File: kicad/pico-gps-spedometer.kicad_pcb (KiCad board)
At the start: 2 copper layers, 19 parts, among them J1 Akkumulátor be, J2 TP4056-18650-Charger, J3 uBlox NEO GPS (6M/8M), Q1 PN2222A, U1 RP2040-ZERO, U2 DS18B20, U3 LM7805_TO220, U4 TFT_320x240

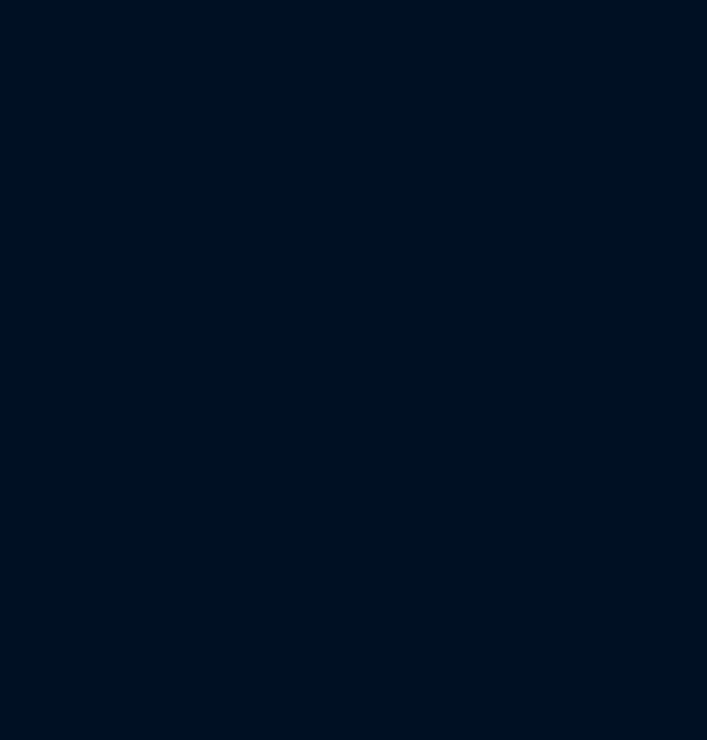
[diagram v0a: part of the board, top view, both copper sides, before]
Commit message: Add TFT backlight adjustment and utility functions
- Implemented TftBackLightAdjuster for dynamic LED backlight control based on ambient light sensor readings.
- Added utility functions for TFT touch calibration and sound feedback (beepTick and beepError) in Utils.cpp.
- Included necessary headers and defined constants for sensor thresholds and brightness levels.
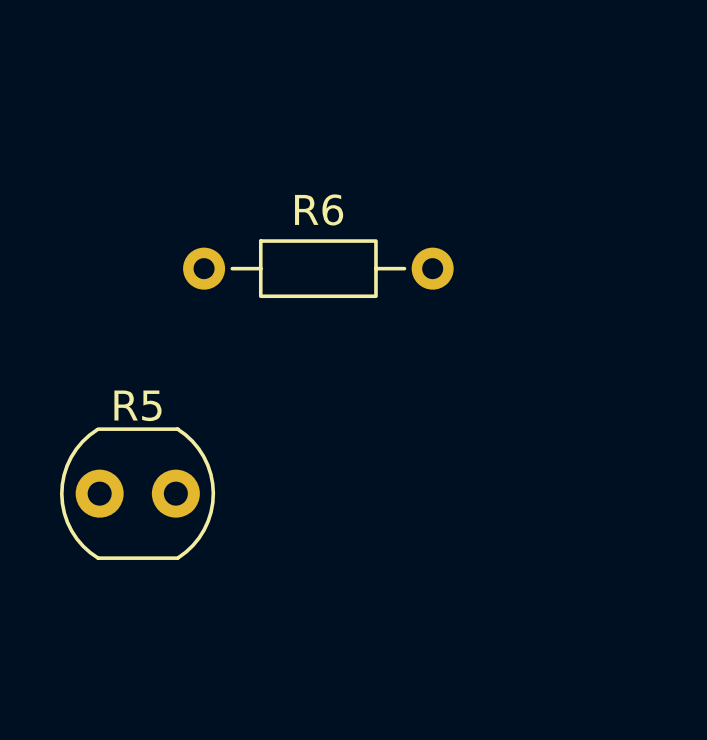
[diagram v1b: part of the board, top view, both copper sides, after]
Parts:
- added R5: GL5516, OptoDevice:R_LDR_4.9x4.2mm_P2.54mm_Vertical, F.Cu at (91.5, 110.0)
- added R6: 10k, Resistor_THT:R_Axial_DIN0204_L3.6mm_D1.6mm_P7.62mm_Horizontal, F.Cu at (94.9, 102.5)
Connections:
- U1 pad 18: unconnected-(U1-GP27-Pad18) -> Net-(U1-GP27)

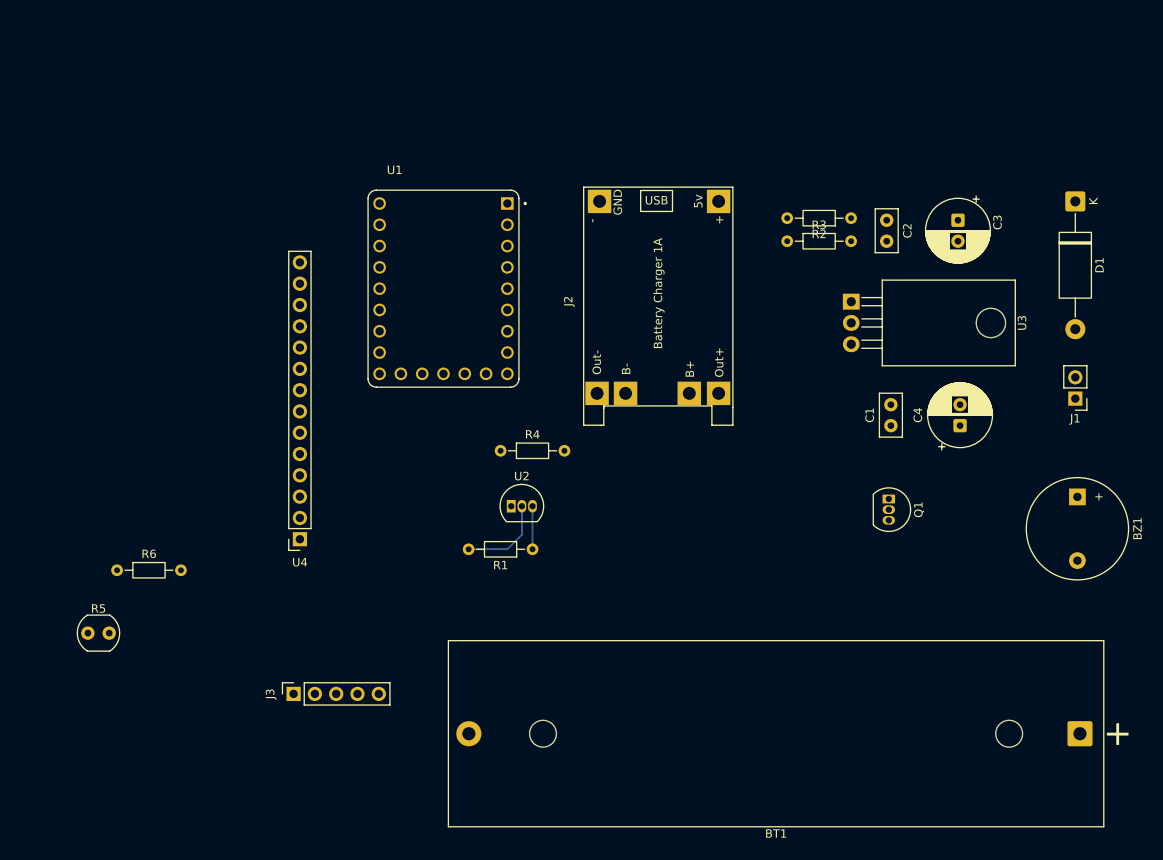
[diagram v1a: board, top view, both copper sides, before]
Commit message: egyoldalas nyák
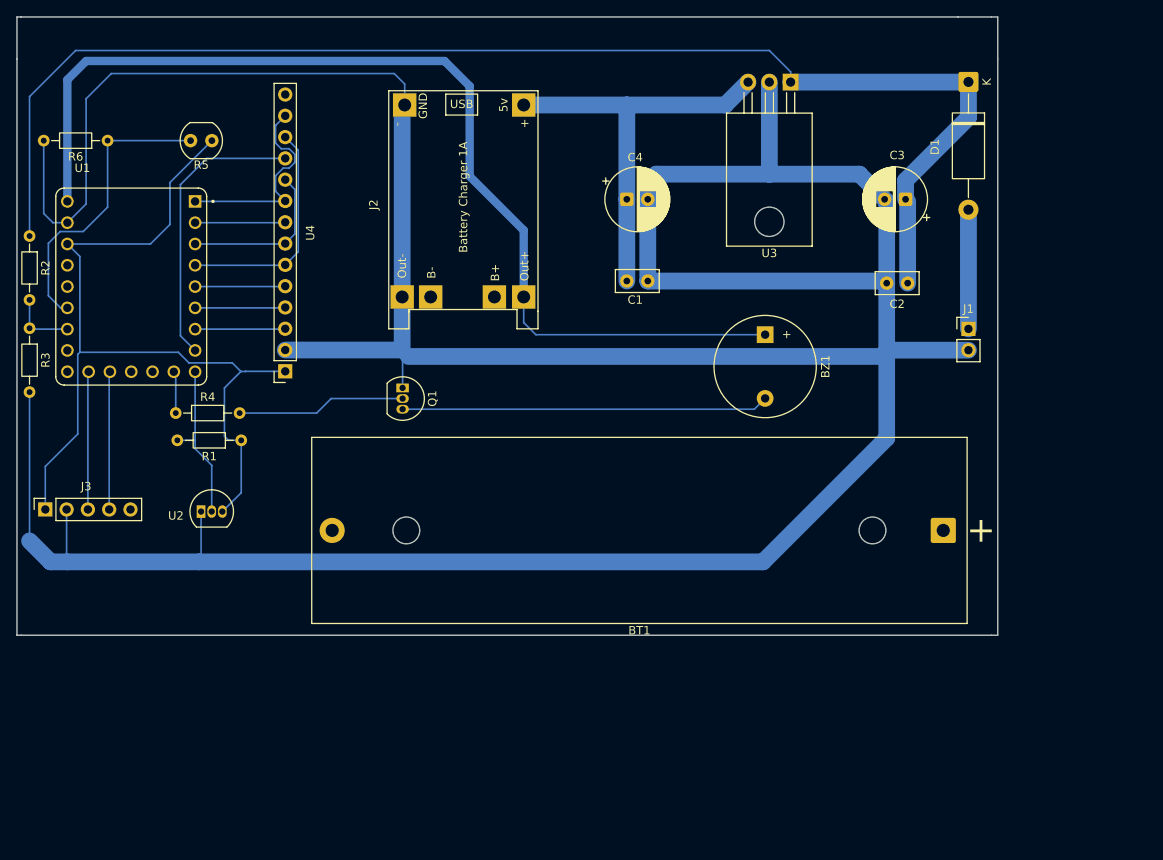
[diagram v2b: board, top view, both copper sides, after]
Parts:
- moved R2 98.0 mm to (84.5, 62.6), turned to -90 degrees
- moved R3 91.0 mm to (84.5, 73.6), turned to -90 degrees
- moved R5 60.6 mm to (106.2, 51.2), turned to 180 degrees
- moved Q1 59.5 mm to (129.0, 80.8)
- moved R6 51.3 mm to (93.8, 51.2), turned to 180 degrees
- moved C4 48.1 mm to (155.8, 58.2), turned to 0 degrees
- moved BZ1 42.0 mm to (172.2, 74.4)
- moved R4 39.0 mm to (101.9, 83.8)
- moved U1 37.3 mm to (96.6, 68.7)
- moved R1 37.1 mm to (109.8, 87.0)
- moved U2 37.0 mm to (105.0, 95.5)
- moved J3 36.9 mm to (86.4, 95.2)
- moved C1 35.9 mm to (155.8, 68.0), turned to 0 degrees
- moved BT1 29.2 mm to (193.5, 97.8)
- moved U3 27.2 mm to (175.3, 44.3), turned to 180 degrees
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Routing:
- net GND: track 0.00 -> 435.4 mm
- net V-IN-MEAS: track 0.00 -> 160.4 mm
- net +5VBATT: track 0.00 -> 124.9 mm
- net +3V3: track 5.14 -> 104.9 mm
- net +5V: track 0.00 -> 48.9 mm
- net Net-(BZ1--): track 0.00 -> 43.8 mm
- net Net-(U1-GP27): track 0.00 -> 35.8 mm
- net /T_CS: track 0.00 -> 34.3 mm
- net /MOSI: track 0.00 -> 27.3 mm
- net /MISO: track 0.00 -> 24.8 mm
- net Net-(Q1-B): track 0.00 -> 20.2 mm
- net /SCK: track 0.00 -> 19.3 mm
- net GPS_RXD: track 0.00 -> 16.7 mm
- net GPS_TXD: track 0.00 -> 16.5 mm
- net Net-(D1-A): track 0.00 -> 14.2 mm
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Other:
- board outline added: 117 x 73.8 mm
